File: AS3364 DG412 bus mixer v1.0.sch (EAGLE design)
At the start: 150 parts, among them IC1 PCA9539PW, IC10 DG412-J, IC11 DG412-J, IC14 TL074JT, IC2 TL074JT, IC3 TL072JT, IC4 TL074JT, IC6 TL072JT, IC8 DG412-J, IC9 DG412-J

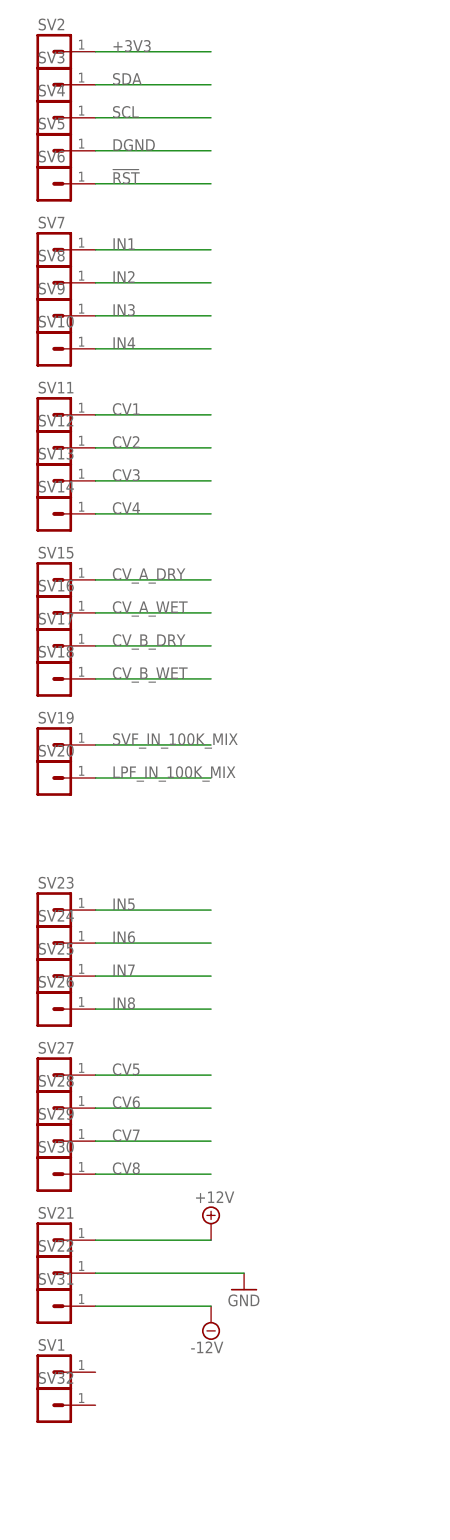
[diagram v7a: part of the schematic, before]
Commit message: Replaced connectors
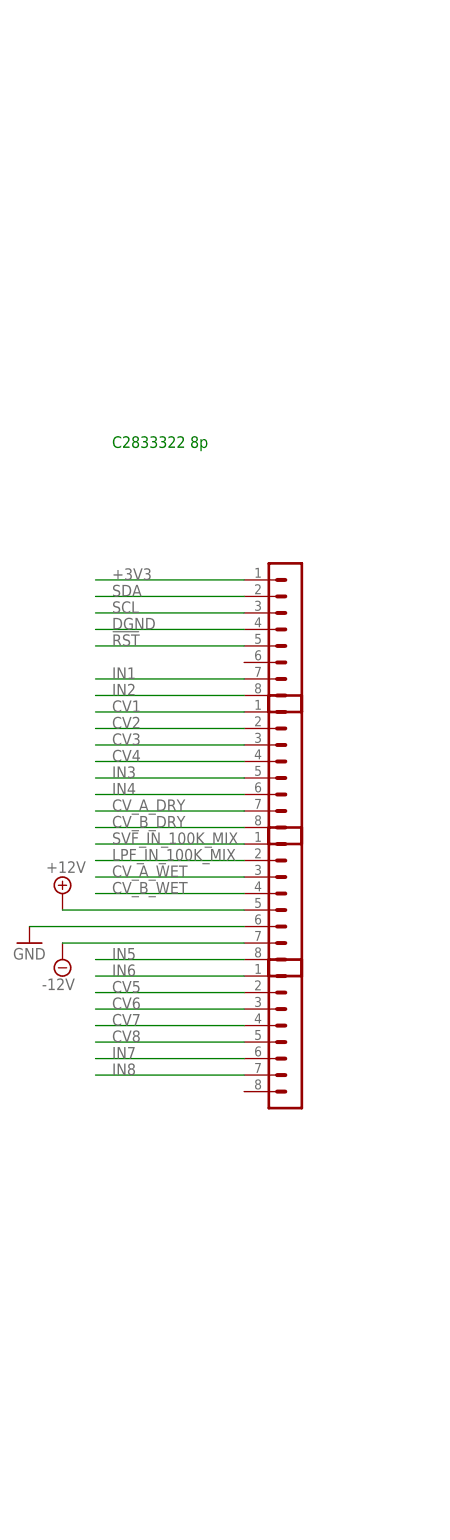
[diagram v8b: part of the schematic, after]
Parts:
- removed SV1, SV10, SV11, SV12, SV13, SV14, SV15, SV16, SV17, SV18, SV19, SV20, SV21, SV22, SV23, SV24, SV25, SV26, SV27, SV28, SV29, SV3, SV30, SV31, SV32, SV4, SV5, SV6, SV7, SV8, SV9: (no value), joakim:MA01-1JP
- added SV33, SV34, SV35: (no value), joakim:MA08-1JP
- SV2: device joakim:MA01-1JP -> joakim:MA08-1JP
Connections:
- net !RST: now also SV33.5; no longer SV6.1
- net +12V: now also SV35.5; no longer SV21.1
- net +3V3: now also SV33.1; no longer SV2.1
- net -12V: now also SV35.7; no longer SV31.1
- net CV1: now also SV34.1; no longer SV11.1
- net CV2: now also SV34.2; no longer SV12.1
- net CV3: now also SV34.3; no longer SV13.1
- net CV4: now also SV34.4; no longer SV14.1
- net CV5: now also SV2.2; no longer SV27.1
- net CV6: now also SV2.3; no longer SV28.1
- net CV7: now also SV2.4; no longer SV29.1
- net CV8: now also SV2.5; no longer SV30.1
- net CV_A_DRY: now also SV34.7; no longer SV15.1
- net CV_A_WET: now also SV35.3; no longer SV16.1
- net CV_B_DRY: now also SV34.8; no longer SV17.1
- net CV_B_WET: now also SV35.4; no longer SV18.1
- net DGND: now also SV33.4; no longer SV5.1
- net GND: now also SV35.6; no longer SV22.1
- net IN1: now also SV33.7; no longer SV7.1
- net IN2: now also SV33.8; no longer SV8.1
- net IN3: now also SV34.5; no longer SV9.1
- net IN4: now also SV34.6; no longer SV10.1
- net IN5: now also SV35.8; no longer SV23.1
- net IN6: now also SV2.1; no longer SV24.1
- net IN7: now also SV2.6; no longer SV25.1
- net IN8: now also SV2.7; no longer SV26.1
- net LPF_IN_100K_MIX: now also SV35.2; no longer SV20.1
- net SCL: now also SV33.3; no longer SV4.1
- net SDA: now also SV33.2; no longer SV3.1
- net SVF_IN_100K_MIX: now also SV35.1; no longer SV19.1
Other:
- note added: "C2833322 8p"
